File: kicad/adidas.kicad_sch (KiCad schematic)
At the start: 21 parts, among them J1 ISP Header, J2 Conn_01x02_Female, J3 SAO Header, U1 MPU-6050, U2 ATTINY841-SSU

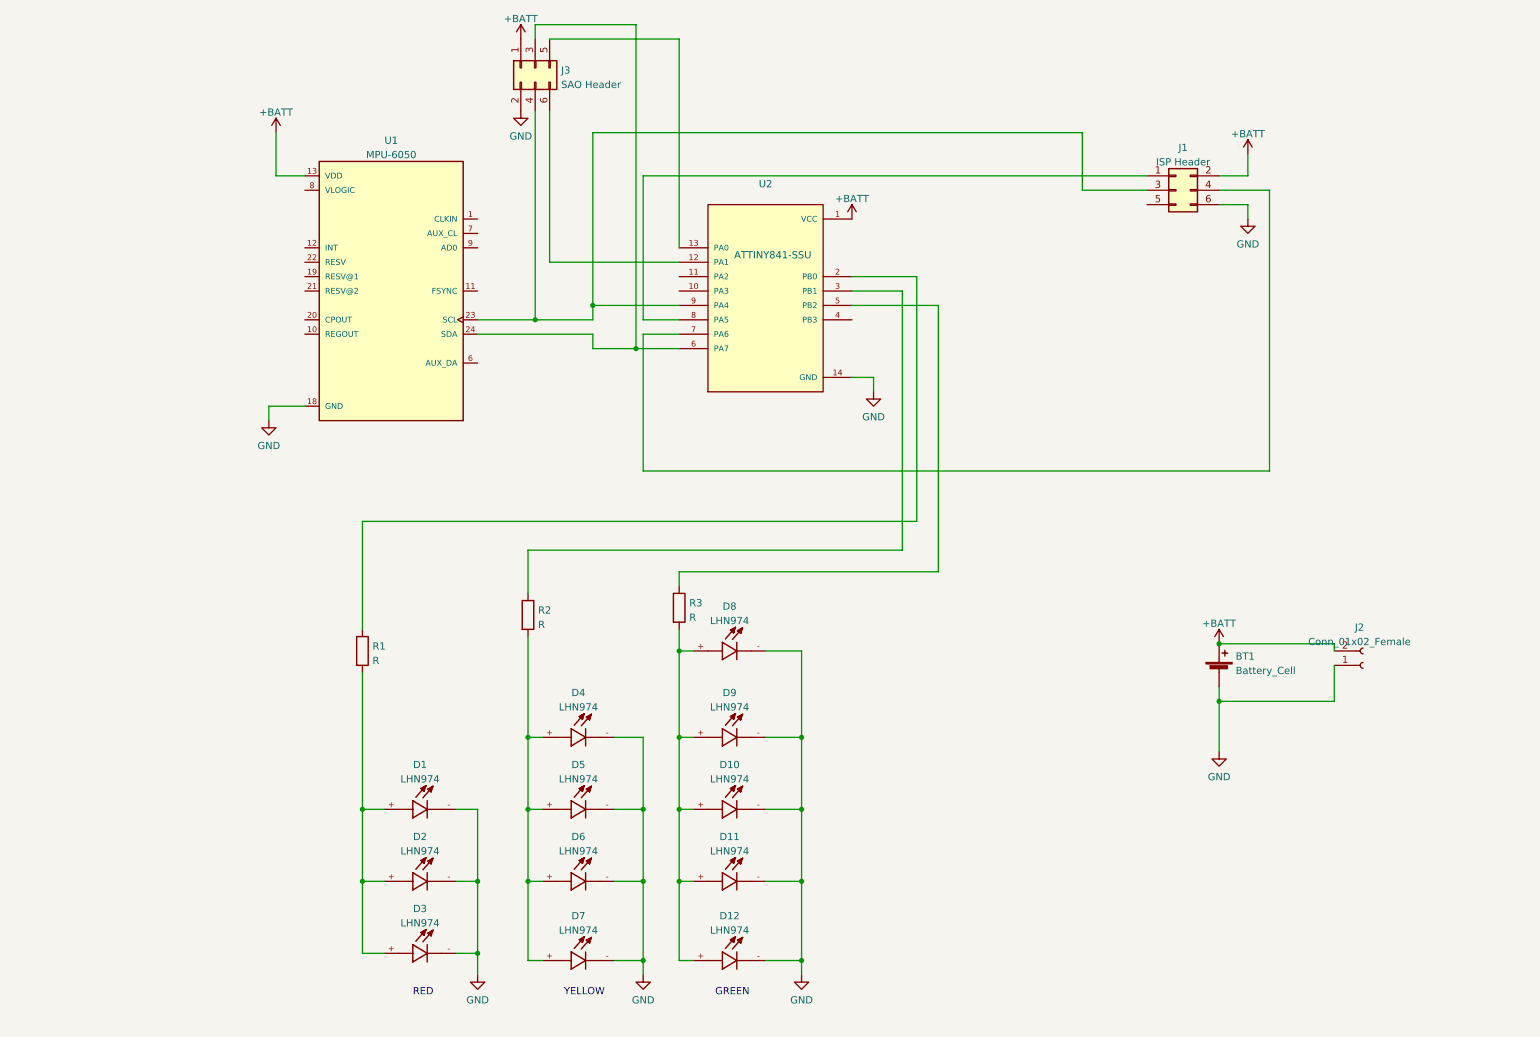
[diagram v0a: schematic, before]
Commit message: code for the board (#23)
* code for the board

* generate 3d front and back images

* changes after feedback from PCBway

* make more updates after PCBway feedback
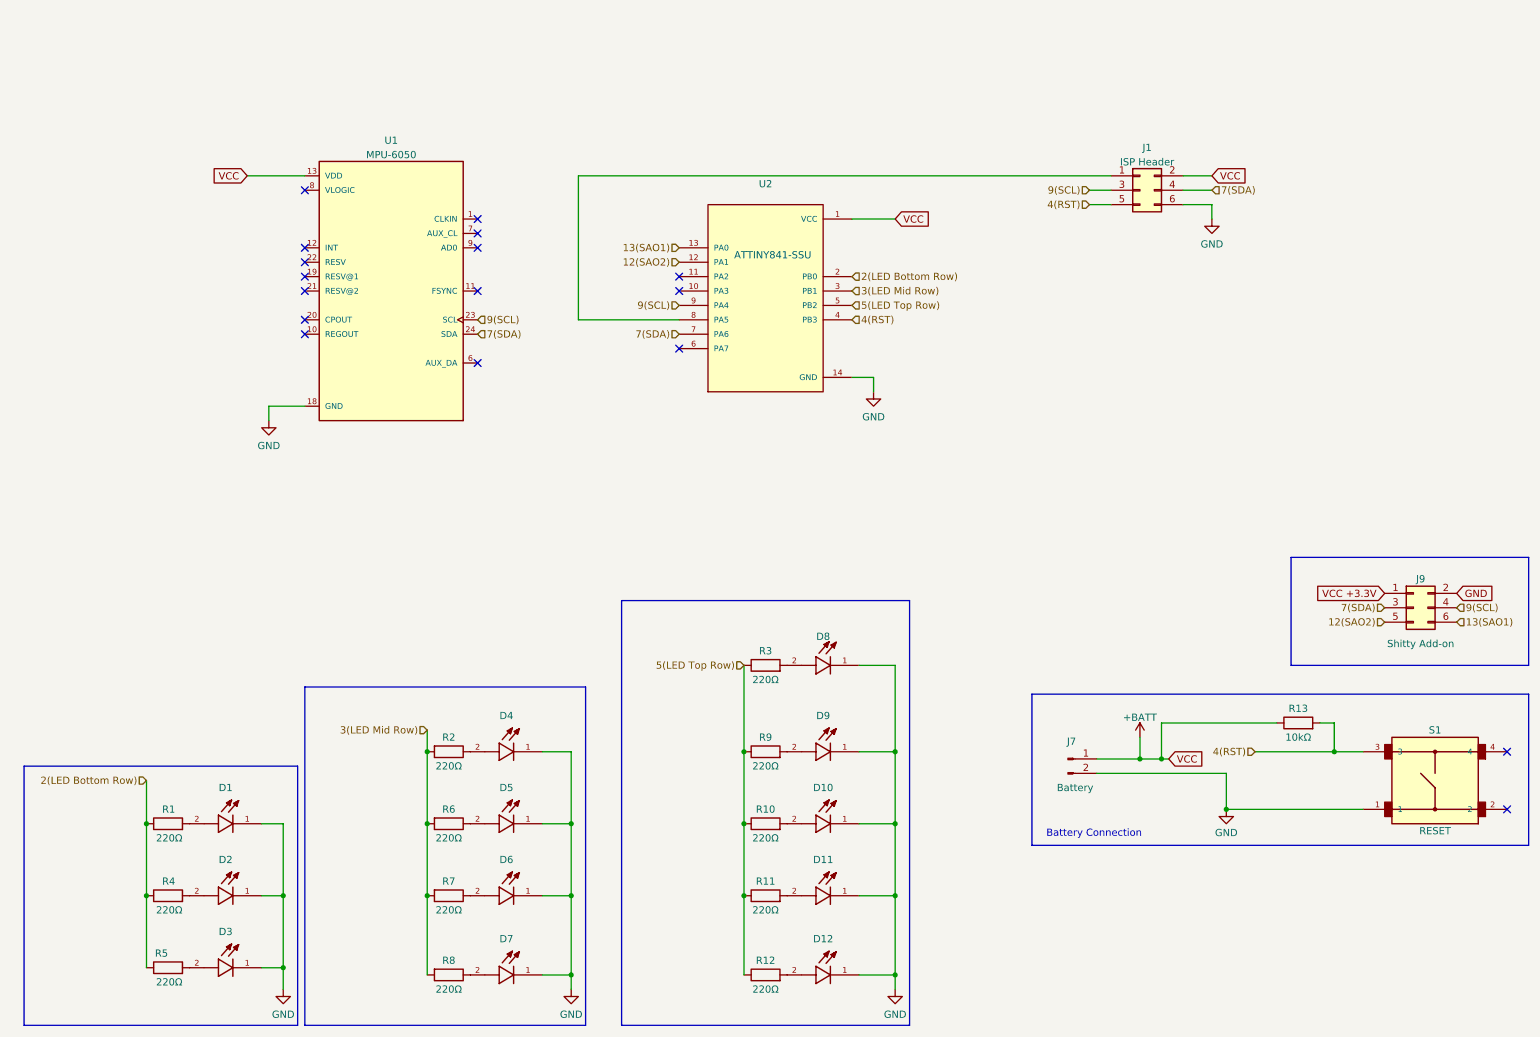
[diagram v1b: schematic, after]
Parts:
- removed BT1: Battery_Cell, Battery:BatteryHolder_Keystone_3002_1x2032, symbol Device:Battery_Cell
- removed J2: Conn_01x02_Female, TestPoint:TestPoint_2Pads_Pitch2.54mm_Drill0.8mm, symbol Connector:Conn_01x02_Female
- removed J3: SAO Header, Connector_PinHeader_2.54mm:PinHeader_2x03_P2.54mm_Vertical, symbol Connector_Generic:Conn_02x03_Odd_Even
- added J7: Battery, Connector_PinSocket_2.54mm:PinSocket_1x02_P2.54mm_Vertical, symbol Connector:Conn_01x02_Pin
- added J9: Shitty Add-on, Connector_PinHeader_2.54mm:PinHeader_2x03_P2.54mm_Vertical, symbol Connector_Generic:Conn_02x03_Odd_Even
- added R10, R11, R12, R4, R5, R6, R7, R8, R9: 220Ω, Resistor_SMD:R_1206_3216Metric, symbol Device:R
- added R13: 10kΩ, Resistor_SMD:R_1206_3216Metric, symbol Device:R
- added S1: B3F-1000, DEAD10C5:SW_B3F-1000, symbol dead10c5:B3F-1000
- D1, D10, D12, D2, D3, D4, D5, D6, D7, D8, D9: footprint 1206_smt:LEDC3216X120N -> LED_SMD:LED_0805_2012Metric; symbol LHN974:LHN974 -> dead10c5:LED-SMD-0805; MANUFACTURER Osram -> Valcon; MAXIMUM_PACKAGE_HEIGHT 1.20mm -> 0.8mm; PARTREV 2002-04-11 -> A; STANDARD IPC7-351B -> Manufacturer Recommendations
- D11: value LHN974 -> ~; footprint 1206_smt:LEDC3216X120N -> LED_SMD:LED_0805_2012Metric; symbol LHN974:LHN974 -> dead10c5:LED-SMD-0805; MANUFACTURER Osram -> Valcon; MAXIMUM_PACKAGE_HEIGHT 1.20mm -> 0.8mm; PARTREV 2002-04-11 -> A; STANDARD IPC7-351B -> Manufacturer Recommendations
- J1: now left out of the parts list
- R1, R2, R3: value R -> 220Ω; footprint Resistor_SMD:R_1206_3216Metric_Pad1.30x1.75mm_HandSolder -> Resistor_SMD:R_1206_3216Metric
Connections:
- net +BATT: now also J7.1 (Pin_1), R13.1
- net GND: now also D1.1, D10.1, D11.1, D12.1, D2.1, D3.1, D4.1, D5.1, D6.1, D7.1, D8.1, D9.1, J7.2 (Pin_2), J9.2 (Pin_2), S1.1; no longer D1.-, D10.-, D11.-, D12.-, D2.-, D3.-, D4.-, D5.-, D6.-, D7.-, D8.-, D9.-
- net 2(LED Bottom Row): now reaches R1.1, U2.2 (PB0)
- net 2(LED Bottom Row): now also R4.1, R5.1
- net at R2.1: now also D4.2; no longer U2.3 (PB1)
- net 9(SCL): now reaches J1.3 (Pin_3), U1.23 (SCL), U2.9 (PA4)
- net 9(SCL): now also J9.4 (Pin_4)
- net 7(SDA): now reaches J1.4 (Pin_4), U2.7 (PA6)
- net 7(SDA): now also U1.24 (SDA), J9.3 (Pin_3)
- net 4(RST): now reaches J1.5 (Pin_5)
- net 4(RST): now also U2.4 (PB3), R13.2, S1.3
- net 5(LED Top Row): now reaches R3.1, U2.5 (PB2)
- net 5(LED Top Row): now also R10.1, R11.1, R12.1, R9.1
- net 12(SAO2): now reaches U2.12 (PA1)
- net 12(SAO2): now also J9.5 (Pin_5)
- net 13(SAO1): now reaches U2.13 (PA0)
- net 13(SAO1): now also J9.6 (Pin_6)
- net at U2.6 (PA7): no longer U1.24 (SDA)
- new net: D1.2, R1.2
- new net: D11.2, R11.2
- new net: D8.2, R3.2
- new net: D12.2, R12.2
- new net: D6.2, R7.1
- new net: D5.2, R6.1
- new net: D3.2, R5.2
- new net: D10.2, R10.2
- new net: D2.2, R4.2
- new net: D9.2, R9.2
- new net: D7.2, R8.1
- new net 3(LED Mid Row): R2.2, R6.2, R7.2, R8.2, U2.3 (PB1)
- new net VCC +3.3V: J9.1 (Pin_1)
- no-connect marks 0 -> 17
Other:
- note added: "Battery Connection"
- note removed: "GREEN"
- note removed: "RED"
- note removed: "YELLOW"
- moved on the sheet: J1, R1, R2, R3
